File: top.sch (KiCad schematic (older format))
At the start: 28 parts, among them J1 USB_B_Mini, J2 TC2030_NL, J3 FFC-0.5MM-6POS, J4 Port_1, J5 Port_2, U1 PMIC-LDO-XC6204B332MR_SOT23-5_, U2 LP2985-5.0, U3 ATmega328P-MU, U4 ADXL337, Y1 16MHz

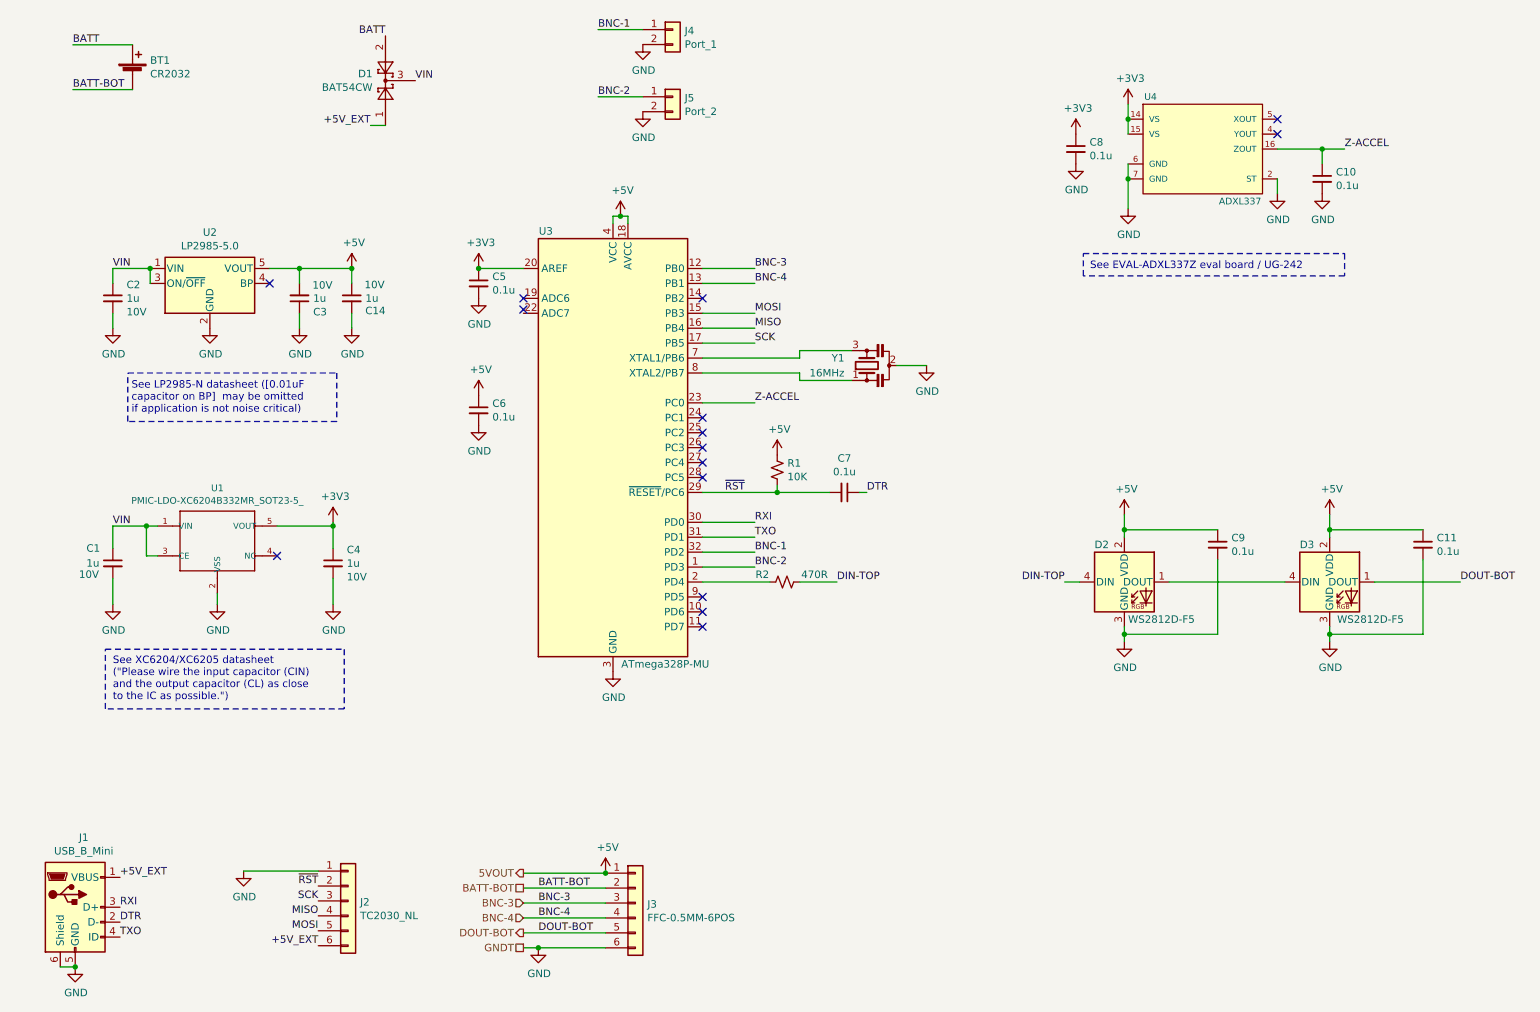
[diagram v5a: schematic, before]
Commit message: Rename nets, fix ERC warnings and errors
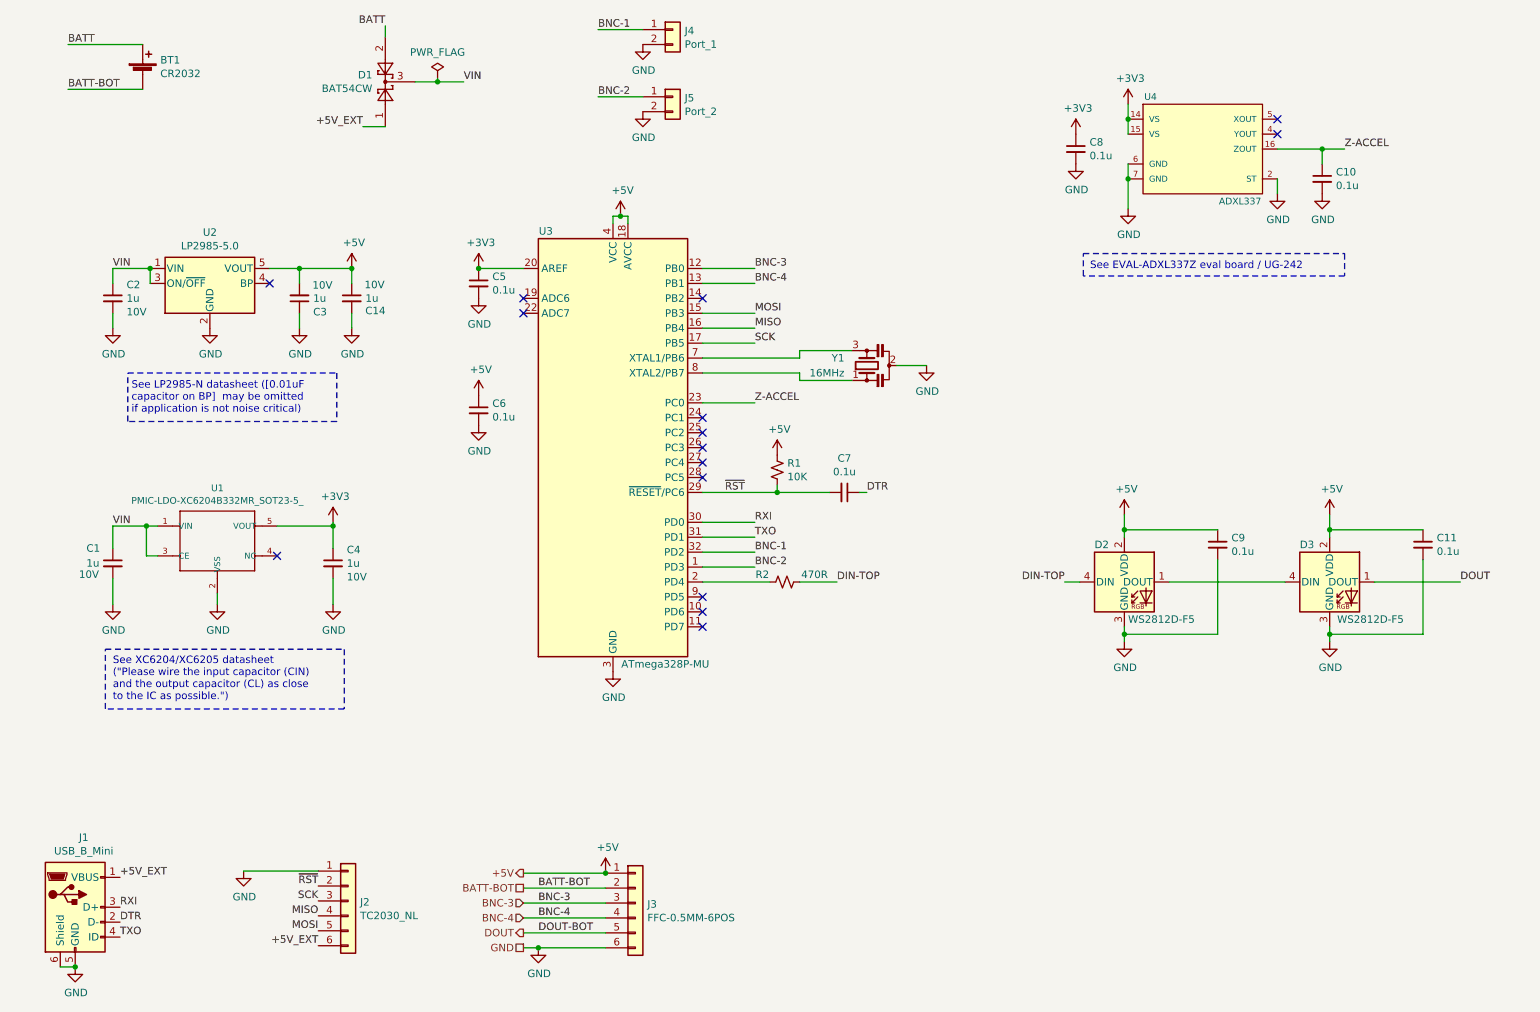
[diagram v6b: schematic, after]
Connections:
- net DOUT-BOT renamed DOUT
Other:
- moved on the sheet: BT1
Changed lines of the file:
@@
 	1    0    0    -1
 $EndComp
-Text HLabel 4000 6950 0    50   UnSpc ~ 0
-GNDT
 Text HLabel 4000 6550 0    50   UnSpc ~ 0
 BATT-BOT
-Text Label 3276 1142 0    50   ~ 0
+Text Label 3600 1150 0    50   ~ 0
 VIN
-$Comp
-L Diode:BAT54CW D?
-U 1 1 5C995166
-P 3076 1142
-AR Path="/5C995166" Ref="D?"  Part="1"
-AR Path="/5C920754/5C995166" Ref="D1"  Part="1"
-F 0 "D1" V 3122 1229 50  0000 L CNN
-F 1 "BAT54CW" V 3031 1229 50  0000 L CNN
-F 2 "Package_TO_SOT_SMD:SOT-323_SC-70" H 3151 1267 50  0001 L CNN
-F 3 "https://assets.nexperia.com/documents/data-sheet/BAT54W_SER.pdf" H 2996 1142 50  0001 C CNN
-F 4 "BAT54C-7-F" H 2026 -1108 50  0001 C CNN "MPN"
-F 5 "BAT54C-7-F" H 2026 -1108 50  0001 C CNN "SKU"
-F 6 "Shenzhen" H 2026 -1108 50  0001 C CNN "OPL"
-F 7 "20" H 2026 -1108 50  0001 C CNN "Min Quantity"
-	1    3076 1142
-	0    -1   -1   0
-$EndComp
 $Comp
 L power:GND #PWR?
@@
 	1    0    0    -1
 $EndComp
-Text Label 3076 842  2    50   ~ 0
+Text Label 3075 775  2    50   ~ 0
 BATT
 Text Label 4500 800  0    50   ~ 0
@@
 Text Label 1298 6478 0    50   ~ 0
 +5V_EXT
-Text Label 2976 1442 2    50   ~ 0
-+5V_EXT
-Wire Wire Line
-	2976 1442 3076 1442
 Text Label 2626 6936 2    50   ~ 0
 +5V_EXT
@@
 L Device:Battery_Cell BT?
 U 1 1 5CA04C70
-P 1382 1102
+P 1450 1100
 AR Path="/5CA04C70" Ref="BT?"  Part="1"
 AR Path="/5C920CA4/5CA04C70" Ref="BT?"  Part="1"
 AR Path="/5C920754/5CA04C70" Ref="BT1"  Part="1"
-F 0 "BT1" H 1500 1198 50  0000 L CNN
-F 1 "CR2032" H 1500 1107 50  0000 L CNN
-F 2 "gsg-modules:BK-912" V 1382 1162 50  0001 C CNN
-F 3 "http://www.memoryprotectiondevices.com/datasheets/BK-912-datasheet.pdf" V 1382 1162 50  0001 C CNN
-F 4 "BK-912" H 382 -198 50  0001 C CNN "MPN"
-F 5 "1" H 382 -198 50  0001 C CNN "Min Quantity"
-	1    1382 1102
-	1    0    0    -1
-$EndComp
-Text Label 982  902  0    50   ~ 0
+F 0 "BT1" H 1568 1196 50  0000 L CNN
+F 1 "CR2032" H 1568 1105 50  0000 L CNN
+F 2 "gsg-modules:BK-912" V 1450 1160 50  0001 C CNN
+F 3 "http://www.memoryprotectiondevices.com/datasheets/BK-912-datasheet.pdf" V 1450 1160 50  0001 C CNN
+F 4 "BK-912" H 450 -200 50  0001 C CNN "MPN"
+F 5 "1" H 450 -200 50  0001 C CNN "Min Quantity"
+	1    1450 1100
+	1    0    0    -1
+$EndComp
+Text Label 950  900  0    50   ~ 0
 BATT
-Text Label 982  1202 0    50   ~ 0
+Text Label 950  1200 0    50   ~ 0
 BATT-BOT
-Wire Wire Line
-	982  902  1382 902
-Wire Wire Line
-	1382 1202 982  1202
 Text Label 4100 6550 0    50   ~ 0
 BATT-BOT
@@
 Z-ACCEL
 Text Label 10275 4500 0    50   ~ 0
-DOUT-BOT
+DOUT
 Text Label 4100 6850 0    50   ~ 0
 DOUT-BOT
 Text HLabel 4000 6850 0    50   Output ~ 0
-DOUT-BOT
+DOUT
 Wire Wire Line
 	4000 6950 4100 6950
@@
 $EndComp
 Text HLabel 4000 6450 0    50   Output ~ 0
-5VOUT
++5V
 Wire Wire Line
 	4000 6450 4550 6450
@@
 NoConn ~ 5200 4800
 NoConn ~ 4000 2600
-NoConn ~ 4000 2675
+NoConn ~ 4000 2700
+Text HLabel 4000 6950 0    50   UnSpc ~ 0
+GND
+$Comp
+L power:PWR_FLAG #FLG0103
+U 1 1 5CA115EA
+P 3425 1125
+F 0 "#FLG0103" H 3425 1200 50  0001 C CNN
+F 1 "PWR_FLAG" H 3425 1298 50  0000 C CNN
+F 2 "" H 3425 1125 50  0001 C CNN
+F 3 "~" H 3425 1125 50  0001 C CNN
+	1    3425 1125
+	1    0    0    -1
+$EndComp
+Text Label 2925 1450 2    50   ~ 0
++5V_EXT
+Wire Wire Line
+	3075 1450 2925 1450
+Wire Wire Line
+	3275 1150 3425 1150
+Wire Wire Line
+	3425 1125 3425 1150
+Connection ~ 3425 1150
+Wire Wire Line
+	3425 1150 3600 1150
+$Comp
+L Diode:BAT54CW D?
+U 1 1 5C995166
+P 3075 1150
+AR Path="/5C995166" Ref="D?"  Part="1"
+AR Path="/5C920754/5C995166" Ref="D1"  Part="1"
+F 0 "D1" V 3121 1237 50  0000 L CNN
+F 1 "BAT54CW" V 3030 1237 50  0000 L CNN
+F 2 "Package_TO_SOT_SMD:SOT-323_SC-70" H 3150 1275 50  0001 L CNN
+F 3 "https://assets.nexperia.com/documents/data-sheet/BAT54W_SER.pdf" H 2995 1150 50  0001 C CNN
+F 4 "BAT54C-7-F" H 2025 -1100 50  0001 C CNN "MPN"
+F 5 "BAT54C-7-F" H 2025 -1100 50  0001 C CNN "SKU"
+F 6 "Shenzhen" H 2025 -1100 50  0001 C CNN "OPL"
+F 7 "20" H 2025 -1100 50  0001 C CNN "Min Quantity"
+	1    3075 1150
+	0    -1   -1   0
+$EndComp
+Wire Wire Line
+	3075 850  3075 775
+Wire Wire Line
+	950  900  1450 900
+Wire Wire Line
+	1450 1200 950  1200
 $EndSCHEMATC

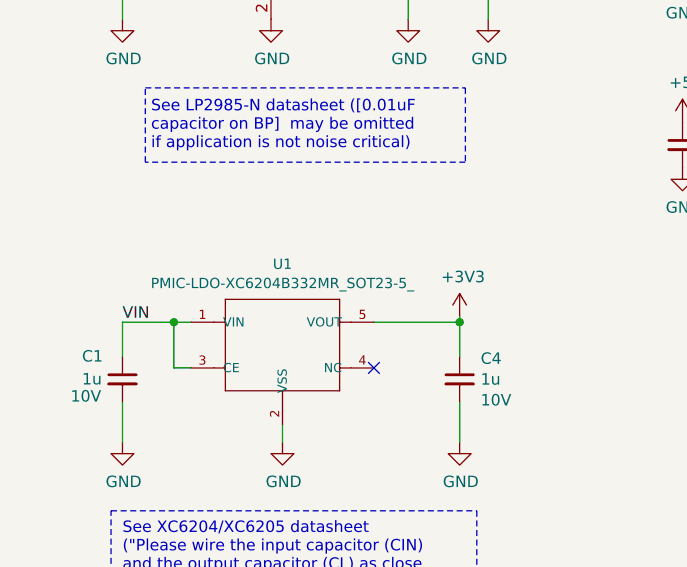
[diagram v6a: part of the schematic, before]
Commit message: Correct pin types in 5V LDO symbol
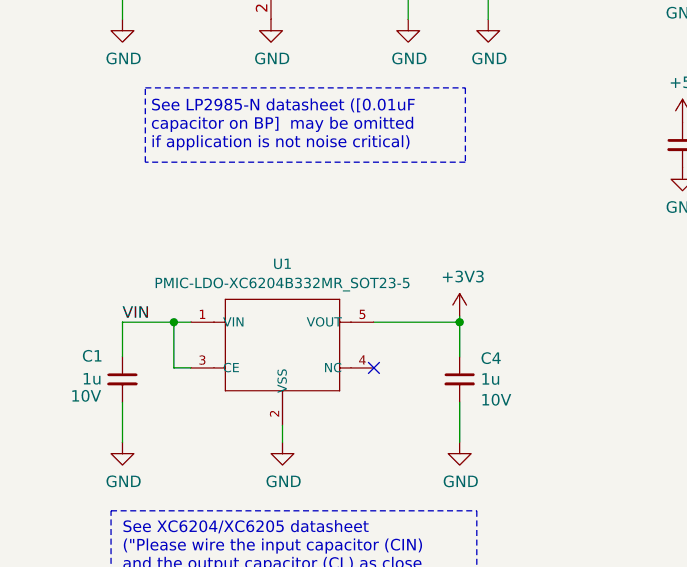
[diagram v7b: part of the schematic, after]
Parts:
- removed U1: PMIC-LDO-XC6204B332MR_SOT23-5_, Package_TO_SOT_SMD:SOT-23-5, symbol OPL_Integrated_Circuit:PMIC-LDO-XC6204B332MR_SOT23-5_
- added U1: PMIC-LDO-XC6204B332MR_SOT23-5, symbol node:PMIC-LDO-XC6204B332MR_SOT23-5
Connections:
- net +3V3: now also U1.5 (VOUT)
- net GND: now also U1.2 (VSS)
- net VIN: now also U1.1 (VIN), U1.3 (CE)
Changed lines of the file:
@@
 	2725 4125 2725 4275
 NoConn ~ 2350 4325
-$Comp
-L OPL_Integrated_Circuit:PMIC-LDO-XC6204B332MR_SOT23-5_ U?
-U 1 1 5C956673
-P 1950 4225
-AR Path="/5C956673" Ref="U?"  Part="1"
-AR Path="/5C920754/5C956673" Ref="U1"  Part="1"
-F 0 "U1" H 1950 4579 45  0000 C CNN
-F 1 "PMIC-LDO-XC6204B332MR_SOT23-5_" H 1950 4495 45  0000 C CNN
-F 2 "Package_TO_SOT_SMD:SOT-23-5" H 1950 4225 50  0001 C CNN
-F 3 "" H 1950 4225 50  0001 C CNN
-F 4 "XC6204B332MR" H 1980 4375 20  0001 C CNN "MPN"
-F 5 "310030046" H 1980 4375 20  0001 C CNN "SKU"
-F 6 "Seeed" H -300 2025 50  0001 C CNN "OPL"
-F 7 "1" H -300 2025 50  0001 C CNN "Min Quantity"
-	1    1950 4225
-	1    0    0    -1
-$EndComp
 Wire Wire Line
 	1550 4125 1475 4125
@@
 Wire Wire Line
 	1450 1200 950  1200
+$Comp
+L node:PMIC-LDO-XC6204B332MR_SOT23-5 U1
+U 1 1 5CA52E37
+P 1950 4225
+F 0 "U1" H 1950 4579 45  0000 C CNN
+F 1 "PMIC-LDO-XC6204B332MR_SOT23-5" H 1950 4495 45  0000 C CNN
+F 2 "" H 1950 4225 50  0001 C CNN
+F 3 "" H 1950 4225 50  0001 C CNN
+F 4 "XC6204B332MR" H 1980 4375 20  0001 C CNN "MPN"
+F 5 "310030046" H 1980 4375 20  0001 C CNN "SKU"
+	1    1950 4225
+	1    0    0    -1
+$EndComp
 $EndSCHEMATC

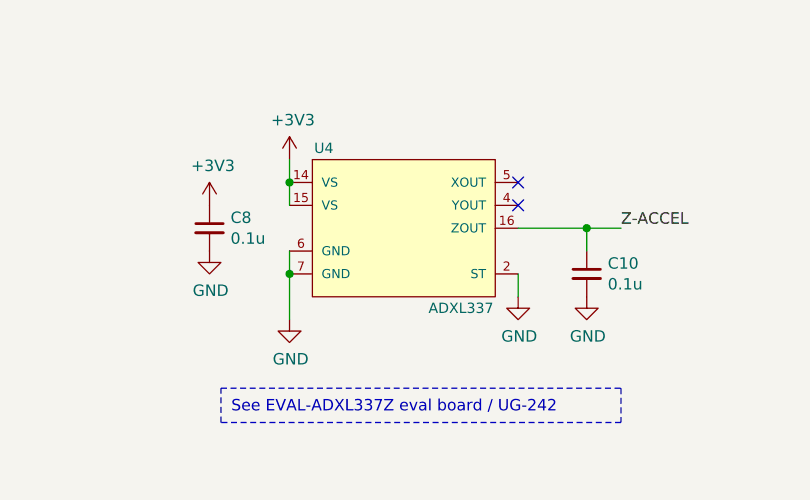
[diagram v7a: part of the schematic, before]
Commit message: Set footprint for ADXL337
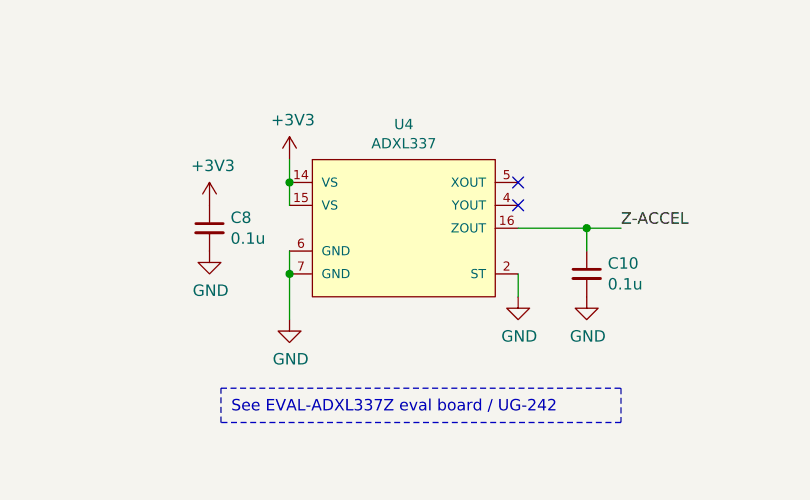
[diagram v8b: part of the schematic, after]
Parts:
- U4: footprint LFCSP-16-3X3 -> Package_CSP:LFCSP-16-1EP_3x3mm_P0.5mm_EP1.6x1.6mm
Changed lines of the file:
@@
 	8050 1300 8050 1400
 Connection ~ 8050 1400
-$Comp
-L node:ADXL337 U4
-U 1 1 5C9E1293
-P 8550 1600
-F 0 "U4" H 8200 1950 45  0000 C CNN
-F 1 "ADXL337" H 8800 1250 45  0000 C CNN
-F 2 "LFCSP-16-3X3" H 8550 2000 20  0001 C CNN
-F 3 "" H 8550 1600 60  0001 C CNN
-	1    8550 1600
-	1    0    0    -1
-$EndComp
 NoConn ~ 5200 2600
 NoConn ~ 5200 3400
@@
 	1    0    0    -1
 $EndComp
+$Comp
+L node:ADXL337 U4
+U 1 1 5CA5DC36
+P 8550 1600
+F 0 "U4" H 8550 2054 45  0000 C CNN
+F 1 "ADXL337" H 8550 1970 45  0000 C CNN
+F 2 "Package_CSP:LFCSP-16-1EP_3x3mm_P0.5mm_EP1.6x1.6mm" H 8550 2000 20  0001 C CNN
+F 3 "" H 8550 1600 60  0001 C CNN
+	1    8550 1600
+	1    0    0    -1
+$EndComp
